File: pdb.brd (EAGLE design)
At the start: 50 x 115.6 mm, 49 parts, among them Q1 20MHz, Q2 IRFR5305PBF, Q3 IRFR5305PBF, U1 TSR_1-2433, U2 LTC2946CMSPBF, U3 LTC2946CMSPBF, U4 LTC2946CMSPBF, U5 ATMEGA48-20AU, U6 TXB0104, U7 AT30TS74SS8M

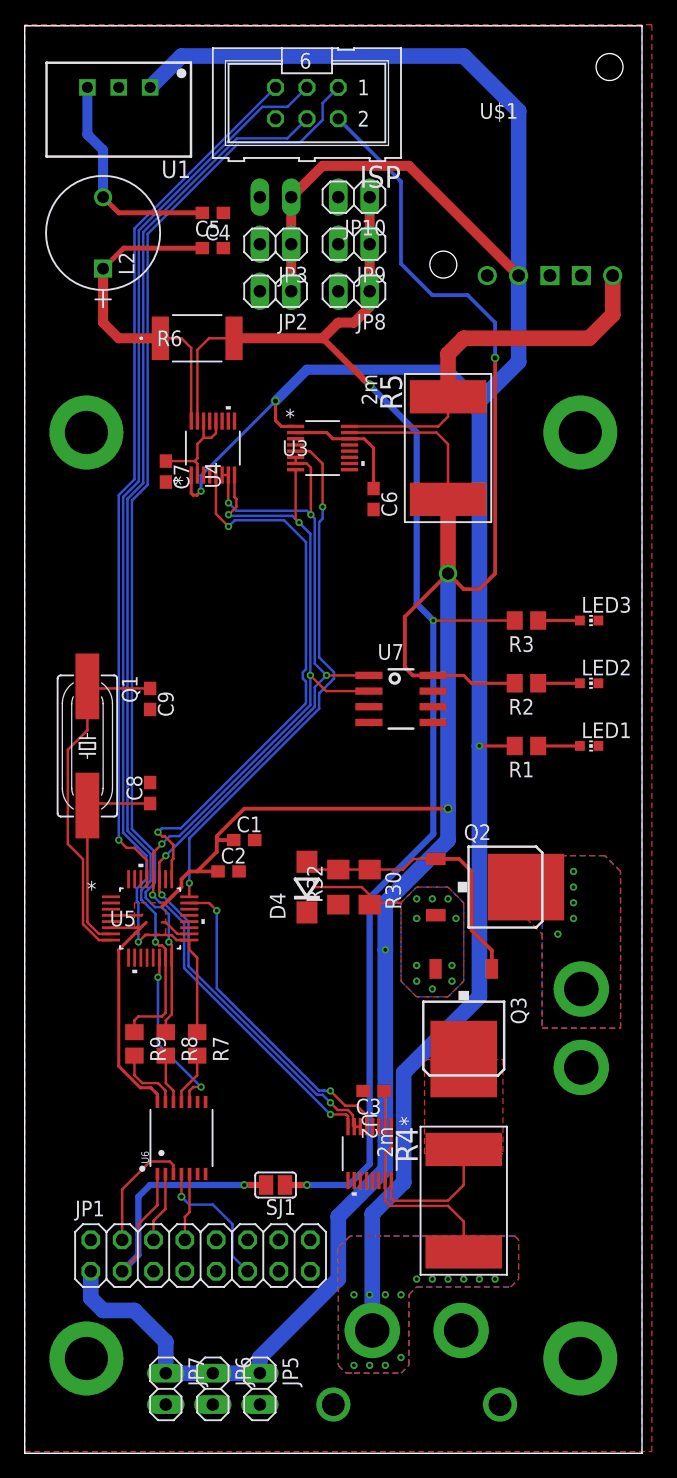
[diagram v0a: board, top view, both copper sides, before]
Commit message: various changes
removed netclasses, might add them later again, creates issues with sense lines
fixed output pin
version bump
fixed some vias/drills
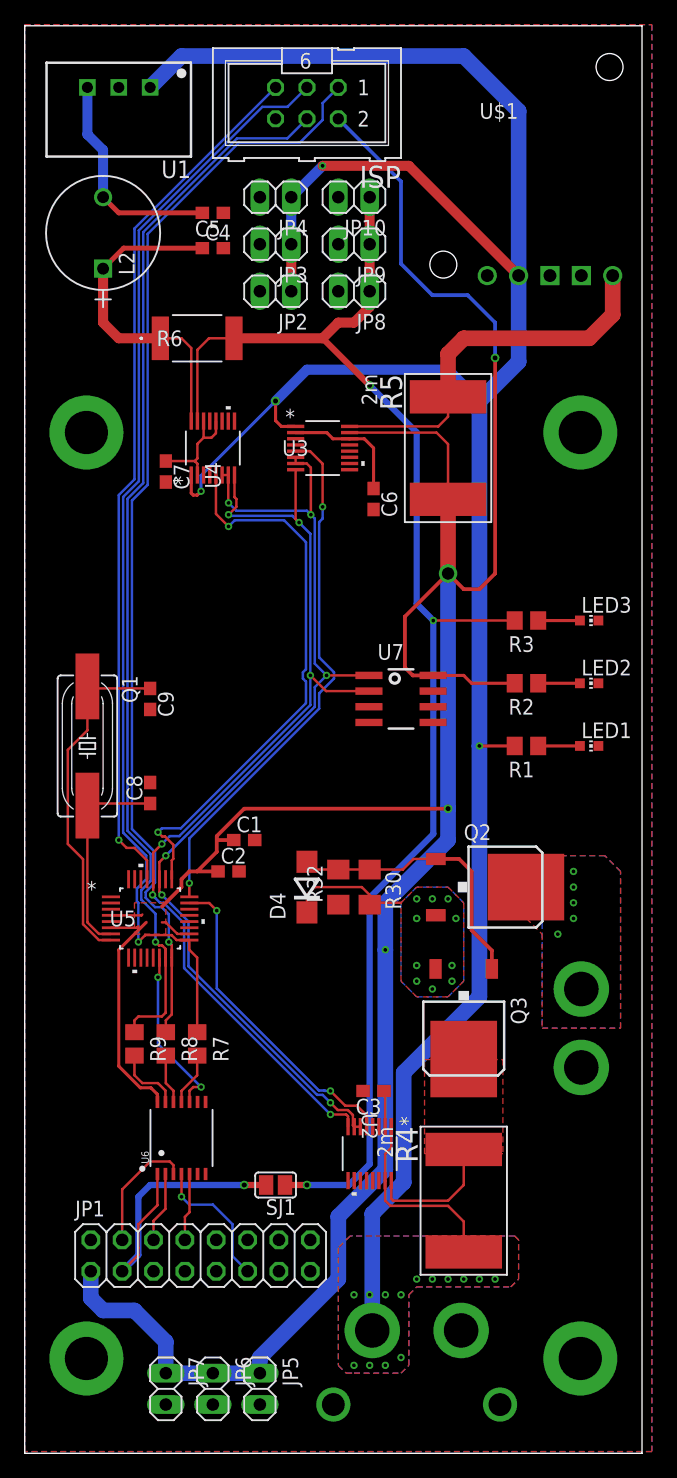
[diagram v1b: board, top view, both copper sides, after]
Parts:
- flipped JP4 to the top, turned to 180 degrees
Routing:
- net V+: vias 17 -> 18
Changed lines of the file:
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@@
 <?xml version="1.0" encoding="utf-8"?>
 <!DOCTYPE eagle SYSTEM "eagle.dtd">
-<eagle version="8.6.1">
+<eagle version="8.6.2">
 <drawing>
 <settings>
@@
 <element name="JP2" library="pinhead" library_urn="urn:adsk.eagle:library:325" package="1X02" package3d_urn="urn:adsk.eagle:package:22435/2" value="" x="20.32" y="91.44" rot="R180"/>
 <element name="JP3" library="pinhead" library_urn="urn:adsk.eagle:library:325" package="1X02" package3d_urn="urn:adsk.eagle:package:22435/2" value="" x="20.32" y="95.25" rot="R180"/>
-<element name="JP4" library="pinhead" library_urn="urn:adsk.eagle:library:325" package="1X02" package3d_urn="urn:adsk.eagle:package:22435/2" value="" x="20.32" y="99.06" rot="MR0"/>
+<element name="JP4" library="pinhead" library_urn="urn:adsk.eagle:library:325" package="1X02" package3d_urn="urn:adsk.eagle:package:22435/2" value="" x="20.32" y="99.06" rot="R180"/>
 <element name="JP5" library="pinhead" library_urn="urn:adsk.eagle:library:325" package="1X02" package3d_urn="urn:adsk.eagle:package:22435/2" value="" x="19.05" y="2.54" rot="R270"/>
 <element name="JP6" library="pinhead" library_urn="urn:adsk.eagle:library:325" package="1X02" package3d_urn="urn:adsk.eagle:package:22435/2" value="" x="15.24" y="2.54" rot="R270"/>
@@
 <contactref element="U6" pad="7"/>
 <contactref element="ESC" pad="NEG"/>
-<polygon width="0.1524" layer="16" rank="6">
-<vertex x="0" y="112.94"/>
-<vertex x="50" y="112.94"/>
-<vertex x="50" y="-2.68"/>
-<vertex x="0" y="-2.68"/>
-</polygon>
-<via x="5" y="80" extent="1-16" drill="3.5" diameter="6" locked="yes"/>
-<via x="45" y="80" extent="1-16" drill="3.5" diameter="6" locked="yes"/>
-<via x="5" y="5" extent="1-16" drill="3.5" diameter="6" locked="yes"/>
-<via x="45" y="5" extent="1-16" drill="3.5" diameter="6" locked="yes"/>
+<via x="5" y="80" extent="1-16" drill="3.5" diameter="6" alwaysstop="yes" locked="yes"/>
+<via x="45" y="80" extent="1-16" drill="3.5" diameter="6" alwaysstop="yes" locked="yes"/>
+<via x="5" y="5" extent="1-16" drill="3.5" diameter="6" alwaysstop="yes" locked="yes"/>
+<via x="45" y="5" extent="1-16" drill="3.5" diameter="6" alwaysstop="yes" locked="yes"/>
 <contactref element="U7" pad="4"/>
 <contactref element="JP1" pad="2"/>
-<polygon width="0.2032" layer="1" rank="6">
-<vertex x="0" y="-2.54"/>
-<vertex x="50.8" y="-2.54"/>
-<vertex x="50.8" y="113.03"/>
-<vertex x="0" y="113.03"/>
-</polygon>
 <contactref element="ISP" pad="6"/>
-<via x="45.085" y="28.575" extent="1-16" drill="2.8" diameter="4.5"/>
+<via x="45.085" y="28.575" extent="1-16" drill="2.8" diameter="4.5" alwaysstop="yes"/>
 <contactref element="JP3" pad="2"/>
 <contactref element="JP4" pad="2"/>
@@
 <contactref element="JP10" pad="2"/>
 <contactref element="JP8" pad="2"/>
-</signal>
-<signal name="V+" class="1">
+<polygon width="0.2032" layer="1" rank="6">
+<vertex x="0" y="113.03"/>
+<vertex x="50.8" y="113.03"/>
+<vertex x="50.8" y="-2.54"/>
+<vertex x="0" y="-2.54"/>
+</polygon>
+<polygon width="0.2032" layer="16" rank="6">
+<vertex x="0" y="113.03"/>
+<vertex x="50.8" y="113.03"/>
+<vertex x="50.8" y="-2.54"/>
+<vertex x="0" y="-2.54"/>
+</polygon>
+</signal>
+<signal name="V+">
 <contactref element="U$1" pad="2"/>
 <contactref element="U1" pad="1"/>
@@
 <via x="30.48" y="10.16" extent="1-16" drill="0.3"/>
 <wire x1="21.59" y1="91.44" x2="21.59" y2="95.25" width="0.8128" layer="1"/>
-<wire x1="21.59" y1="95.25" x2="21.59" y2="99.06" width="0.8128" layer="1"/>
-<wire x1="21.59" y1="99.06" x2="24.13" y2="101.6" width="0.8128" layer="1"/>
+<wire x1="21.59" y1="95.25" x2="21.59" y2="99.06" width="0.8128" layer="16"/>
+<wire x1="21.59" y1="99.06" x2="24.13" y2="101.6" width="0.8128" layer="16"/>
 <wire x1="24.13" y1="101.6" x2="31.115" y2="101.6" width="0.8128" layer="1"/>
 <wire x1="31.115" y1="101.6" x2="40.005" y2="92.71" width="0.8128" layer="1"/>
-</signal>
-<signal name="+5V" class="4">
+<via x="24.13" y="101.6" extent="1-16" drill="0.3"/>
+</signal>
+<signal name="+5V">
 <contactref element="C1" pad="1"/>
 <contactref element="C2" pad="1"/>
@@
 <wire x1="34.29" y1="46.99" x2="29.21" y2="41.91" width="1.27" layer="16"/>
 <wire x1="29.21" y1="41.91" x2="29.21" y2="38.1" width="1.27" layer="16"/>
-<via x="34.29" y="49.53" extent="1-16" drill="0.45"/>
+<via x="34.29" y="49.53" extent="1-16" drill="0.4"/>
 <wire x1="29.21" y1="38.1" x2="29.21" y2="20.32" width="1.27" layer="16"/>
 <wire x1="34.29" y1="49.53" x2="17.78" y2="49.53" width="0.3048" layer="1"/>
@@
 <wire x1="36.195" y1="44.45" x2="35.185" y2="45.46" width="0.3048" layer="1"/>
 </signal>
-<signal name="AKKU-ZWISCHEN" class="1">
+<signal name="AKKU-ZWISCHEN">
 <contactref element="Q2" pad="3"/>
 <contactref element="D4" pad="C"/>
@@
 <wire x1="28.092" y1="41.91" x2="30.48" y2="41.91" width="0.2032" layer="1"/>
 </signal>
-<signal name="BAT_IN" class="1">
+<signal name="BAT_IN">
 <contactref element="Q2" pad="4"/>
 <via x="44.45" y="44.45" extent="1-16" drill="0.3"/>
@@
 <vertex x="39.37" y="45.72"/>
 </polygon>
-<via x="45.085" y="34.925" extent="1-16" drill="2.8" diameter="4.5"/>
+<via x="45.085" y="34.925" extent="1-16" drill="2.8" diameter="4.5" alwaysstop="yes"/>
 </signal>
 <signal name="N$6">
@@
 <wire x1="7.62" y1="97.79" x2="6.35" y2="99.06" width="0.4064" layer="1"/>
 </signal>
-<signal name="+3V3" class="4">
+<signal name="+3V3">
 <contactref element="R3" pad="2"/>
 <contactref element="U4" pad="15"/>
@@
 <wire x1="33.0962" y1="64.77" x2="31.75" y2="66.1162" width="0.508" layer="16"/>
 <wire x1="31.75" y1="80.01" x2="27.94" y2="83.82" width="0.508" layer="16"/>
-<via x="27.94" y="83.82" extent="1-16" drill="0.5"/>
+<via x="27.94" y="83.82" extent="1-16" drill="0.4"/>
 <wire x1="27.94" y1="83.82" x2="24.13" y2="87.63" width="0.508" layer="1"/>
 <wire x1="31.75" y1="66.1162" x2="31.75" y2="80.01" width="0.508" layer="16"/>
@@
 <contactref element="SJ1" pad="1"/>
 <wire x1="21.082" y1="19.05" x2="22.86" y2="19.05" width="0.508" layer="1"/>
-<via x="22.86" y="19.05" extent="1-16" drill="0.35"/>
+<via x="22.86" y="19.05" extent="1-16" drill="0.4"/>
 <wire x1="26.25170625" y1="19.05" x2="22.86" y2="19.05" width="0.508" layer="16"/>
 <wire x1="27.94" y1="20.73829375" x2="26.25170625" y2="19.05" width="0.508" layer="16"/>
@@
 <wire x1="41.59" y1="64.77" x2="44.97" y2="64.77" width="0.254" layer="1"/>
 </signal>
-<signal name="SENSE+V+" class="4">
+<signal name="SENSE+V+">
 <contactref element="Q3" pad="4"/>
 <contactref element="R4" pad="P$1"/>
@@
 <wire x1="16.8275" y1="13.2925" x2="16.8275" y2="15.875" width="0.2032" layer="16"/>
 <wire x1="15.24" y1="17.4625" x2="16.8275" y2="15.875" width="0.2032" layer="16"/>
-<via x="12.7" y="18.0975" extent="1-16" drill="0.35"/>
+<via x="12.7" y="18.0975" extent="1-16" drill="0.3"/>
 <wire x1="12.7" y1="18.0975" x2="12.7" y2="19.9422" width="0.2032" layer="1"/>
 <wire x1="12.7" y1="18.0975" x2="13.335" y2="17.4625" width="0.2032" layer="16"/>
@@
 <wire x1="12.7" y1="26.67" x2="13.97" y2="27.94" width="0.2032" layer="1"/>
 </signal>
-<signal name="EXT_3V3" class="4">
+<signal name="EXT_3V3">
 <contactref element="JP1" pad="3"/>
 <contactref element="U6" pad="1"/>
@@
 <wire x1="9.2075" y1="18.0975" x2="10.16" y2="19.05" width="0.508" layer="16"/>
 <wire x1="10.16" y1="19.05" x2="17.78" y2="19.05" width="0.508" layer="16"/>
-<via x="17.78" y="19.05" extent="1-16" drill="0.35"/>
+<via x="17.78" y="19.05" extent="1-16" drill="0.4"/>
 <wire x1="17.78" y1="19.05" x2="19.558" y2="19.05" width="0.508" layer="1"/>
 <wire x1="9.2075" y1="13.97" x2="9.2075" y2="13.3775" width="0.2032" layer="1"/>

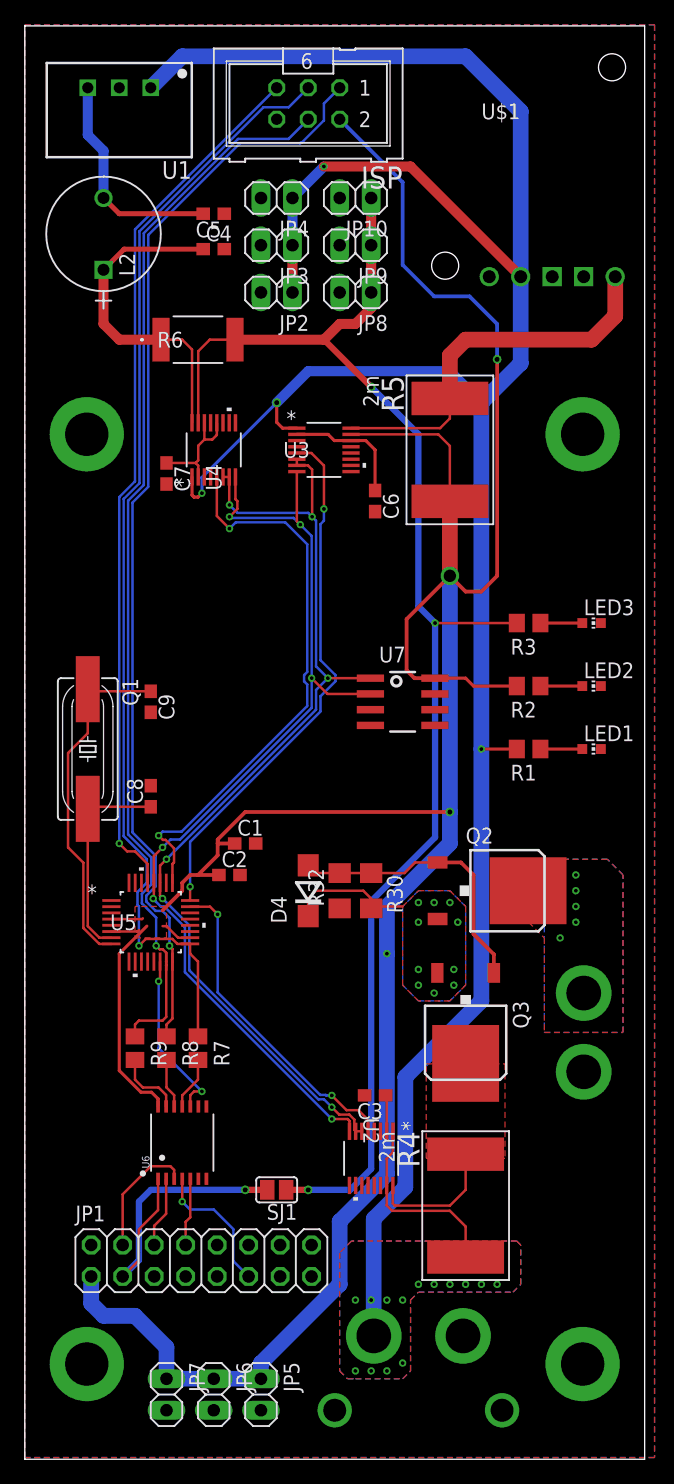
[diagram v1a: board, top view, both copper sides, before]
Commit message: gnd routing
netclasses
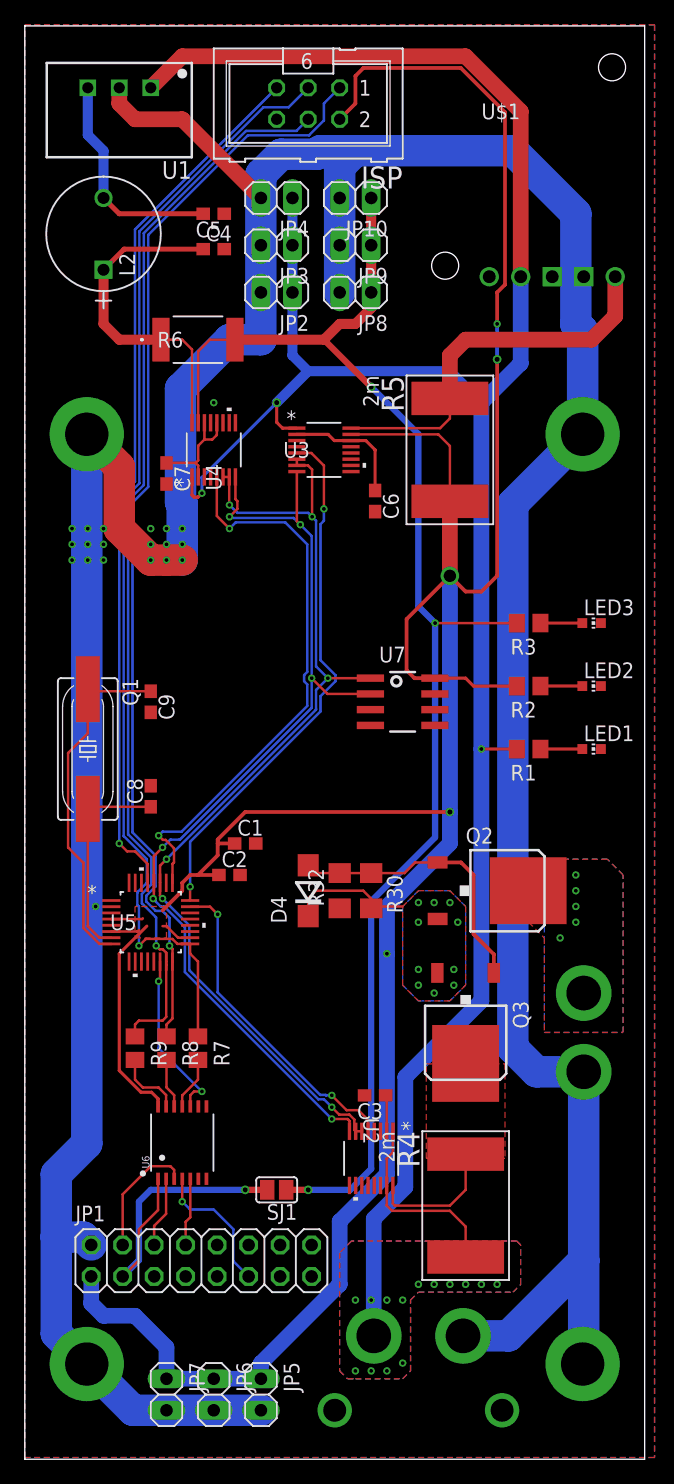
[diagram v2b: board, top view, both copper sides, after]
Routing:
- net GND: track 0.00 -> 315.5 mm, vias 5 -> 25
- net V+: track 220.1 -> 203.8 mm, vias 18 -> 17
- net +5V: track 232.3 -> 244.0 mm, vias 4 -> 5

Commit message: sachen gemacht dass fusion glücklich ist
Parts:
- removed ISP: (no value), con-harting-ml:ML6
- added JP11: (no value), pinhead:2X03/90
- moved JP4 74.4 mm to (94.3, 107.1)
- moved JP2 71.1 mm to (91.3, 87.4)
- moved JP3 70.1 mm to (90.3, 91.2)
- moved JP10 64.0 mm to (90.7, 100.1)
- moved JP8 63.6 mm to (89.7, 82.4)
- moved JP6 58.2 mm to (-12.8, 53.5)
- moved JP7 58.0 mm to (-22.6, 49.5)
- moved JP9 56.6 mm to (80.7, 78.2)
- moved JP5 56.4 mm to (-4.95, 53.5)
- moved C4 35.0 mm to (-5.76, 66.9)
- moved C5 30.0 mm to (-2.76, 73.8)
- moved R6 24.0 mm to (15.0, 63.6)
- moved U1 16.0 mm to (3.05, 92.6), turned to 270 degrees
- moved U$1 13.0 mm to (29.4, 104.2), turned to 270 degrees
- moved L2 8.06 mm to (14.3, 98.1)
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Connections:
- net +5V: now also JP11.2; no longer ISP.2
- net GND: now also JP11.6; no longer ISP.6
- net MISO_5V: now also JP11.1; no longer ISP.1
- net MOSI_5V: now also JP11.4; no longer ISP.4
- net RESET: now also JP11.5; no longer ISP.5
- net SCK_5V: now also JP11.3; no longer ISP.3
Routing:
- net GND: track 315.5 -> 198.9 mm
- net V+: track 203.8 -> 137.1 mm
- net +5V: track 244.0 -> 188.3 mm
- net +3V3: track 116.9 -> 94.0 mm
- net MISO_5V: track 88.9 -> 67.8 mm
- net SENSE+3V3: track 27.0 -> 7.03 mm
- net SCK_5V: track 90.7 -> 72.3 mm
- net N$6: track 18.0 -> 0.00 mm
- net MOSI_5V: track 86.6 -> 69.6 mm
- net RESET: track 70.7 -> 54.6 mm
- net SENSE+5V: track 31.2 -> 25.3 mm
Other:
- board size 50 x 115.6 mm -> 50 x 100 mm

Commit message: layout stuff
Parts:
- removed JP10, JP2, JP3, JP4, JP5, JP6, JP7, JP8, JP9: (no value), pinhead:1X02
- moved C4 36.7 mm to (21.0, 92.0)
- moved C5 33.9 mm to (21.0, 98.0)
- moved R6 19.4 mm to (15.0, 83.0)
- moved C6 9.00 mm to (25.0, 83.0), turned to 0 degrees
- moved U1 4.60 mm to (7.62, 92.1), turned to 90 degrees
- moved U4 2.75 mm to (15.0, 76.0)
- moved U3 1.89 mm to (26.0, 79.0)
- moved C7 1.88 mm to (11.0, 75.0), turned to 90 degrees
- moved Q3 1.33 mm to (36.0, 33.0)
- moved R4 1.30 mm to (36.0, 19.0)
- moved C3 1.00 mm to (28.3, 27.7)
- moved D4 1.00 mm to (22.9, 44.2)
- moved R30 1.00 mm to (27.9, 44.2)
- moved R32 1.00 mm to (25.4, 44.2)
- moved U2 1.00 mm to (27.9, 22.6)
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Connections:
- net +3V3: no longer JP10.1, JP8.1, JP9.1
- net +5V: no longer JP5.1, JP6.1, JP7.1
- net GND: no longer JP10.2, JP2.2, JP3.2, JP4.2, JP5.2, JP6.2, JP7.2, JP8.2, JP9.2
- net V+: no longer JP2.1, JP3.1, JP4.1
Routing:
- net GND: track 198.9 -> 162.1 mm, vias 25 -> 15
- net SCK_5V: track 72.3 -> 38.5 mm, vias 1 -> 2
- net V+: track 137.1 -> 167.7 mm, vias 17 -> 15
- net MISO_5V: track 67.8 -> 41.5 mm, vias 1 -> 2
- net MOSI_5V: track 69.6 -> 48.9 mm, vias 1 -> 3
- net SENSE+3V3: track 7.03 -> 23.6 mm
- net !ALERT_3V3: track 45.9 -> 31.7 mm
- net N$6: track 0.00 -> 13.9 mm
- net RESET: track 54.6 -> 42.5 mm, vias 1 -> 2
- net SENSE+5V: track 25.3 -> 18.0 mm
- net +5V: track 188.3 -> 183.4 mm, vias 5 -> 2
- net AKKU-ZWISCHEN: track 10.4 -> 13.5 mm, vias 10 -> 6
- net INTVCC_5V: track 10.1 -> 7.78 mm
- net +3V3: track 94.0 -> 95.7 mm
- net SENSE+V+: track 10.8 -> 12.2 mm
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- removed copper zone on layer 1, net SENSE+V+
